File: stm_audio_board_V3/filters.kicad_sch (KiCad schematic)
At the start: 26 parts

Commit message: minor commit
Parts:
- removed C52, C53: 100n, Capacitor_SMD:C_0603_1608Metric, symbol Device:C_Small
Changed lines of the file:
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@@
   (junction (at 133.35 54.61) (diameter 0) (color 0 0 0 0)
   )
-  (junction (at 29.21 73.66) (diameter 0) (color 0 0 0 0)
-  )
   (junction (at 180.34 46.99) (diameter 0) (color 0 0 0 0)
   )
@@
   (junction (at 156.21 54.61) (diameter 0) (color 0 0 0 0)
   )
-  (junction (at 29.21 68.58) (diameter 0) (color 0 0 0 0)
-  )
-  (wire (pts (xy 29.21 68.58) (xy 38.1 68.58))
-    (stroke (width 0) (type default))
-  )
   (wire (pts (xy 109.22 48.26) (xy 109.22 46.99))
     (stroke (width 0) (type default))
@@
     (stroke (width 0) (type default))
   )
-  (wire (pts (xy 29.21 73.66) (xy 38.1 73.66))
-    (stroke (width 0) (type default))
-  )
   (wire (pts (xy 144.78 54.61) (xy 156.21 54.61))
     (stroke (width 0) (type default))
@@
     (stroke (width 0) (type default))
   )
-  (wire (pts (xy 26.67 68.58) (xy 29.21 68.58))
-    (stroke (width 0) (type default))
-  )
   (wire (pts (xy 44.45 53.34) (xy 44.45 54.61))
     (stroke (width 0) (type default))
   )
   (wire (pts (xy 133.35 54.61) (xy 144.78 54.61))
-    (stroke (width 0) (type default))
-  )
-  (wire (pts (xy 26.67 73.66) (xy 29.21 73.66))
     (stroke (width 0) (type default))
   )
@@
     )
   )
-  (symbol (lib_id "power:+9V") (at 26.67 68.58 0) (unit 1)
-    (in_bom yes) (on_board yes) (dnp no) (fields_autoplaced)
-    (property "Reference" "#PWR074" (at 26.67 72.39 0)
-      (effects (font (size 1.27 1.27)) hide)
-    )
-    (property "Value" "+9V" (at 26.67 64.77 0)
-      (effects (font (size 1.27 1.27)))
-    )
-    (property "Footprint" "" (at 26.67 68.58 0)
-      (effects (font (size 1.27 1.27)) hide)
-    )
-    (property "Datasheet" "" (at 26.67 68.58 0)
-      (effects (font (size 1.27 1.27)) hide)
-    )
-    (pin "1")
-    (instances
-      (project "stm_audio_board_V3"
-        (path "/6997cf63-2615-4e49-9471-e7da1b6bae71/2eb2ee8f-ab98-4666-97f0-bfacb073bc88"
-          (reference "#PWR074") (unit 1)
-        )
-        (path "/6997cf63-2615-4e49-9471-e7da1b6bae71/927539c8-c0d0-4950-9b67-385a1cdd80f8"
-          (reference "#PWR055") (unit 1)
-        )
-      )
-    )
-  )
   (symbol (lib_id "Device:C_Small") (at 97.79 50.8 0) (unit 1)
     (in_bom yes) (on_board yes) (dnp no) (fields_autoplaced)
@@
     )
   )
-  (symbol (lib_id "Device:C_Small") (at 38.1 71.12 0) (unit 1)
-    (in_bom yes) (on_board yes) (dnp no) (fields_autoplaced)
-    (property "Reference" "C53" (at 40.64 70.4913 0)
-      (effects (font (size 1.27 1.27)) (justify left))
-    )
-    (property "Value" "100n" (at 40.64 73.0313 0)
-      (effects (font (size 1.27 1.27)) (justify left))
-    )
-    (property "Footprint" "Capacitor_SMD:C_0603_1608Metric" (at 38.1 71.12 0)
-      (effects (font (size 1.27 1.27)) hide)
-    )
-    (property "Datasheet" "~" (at 38.1 71.12 0)
-      (effects (font (size 1.27 1.27)) hide)
-    )
-    (pin "1")
-    (pin "2")
-    (instances
-      (project "stm_audio_board_V3"
-        (path "/6997cf63-2615-4e49-9471-e7da1b6bae71"
-          (reference "C53") (unit 1)
-        )
-        (path "/6997cf63-2615-4e49-9471-e7da1b6bae71/927539c8-c0d0-4950-9b67-385a1cdd80f8"
-          (reference "C90") (unit 1)
-        )
-      )
-    )
-  )
   (symbol (lib_id "power:GND") (at 26.67 55.88 0) (unit 1)
     (in_bom yes) (on_board yes) (dnp no) (fields_autoplaced)
@@
     )
   )
-  (symbol (lib_id "Device:C_Small") (at 29.21 71.12 0) (unit 1)
-    (in_bom yes) (on_board yes) (dnp no)
-    (property "Reference" "C52" (at 31.75 70.4913 0)
-      (effects (font (size 1.27 1.27)) (justify left))
-    )
-    (property "Value" "100n" (at 31.75 73.0313 0)
-      (effects (font (size 1.27 1.27)) (justify left))
-    )
-    (property "Footprint" "Capacitor_SMD:C_0603_1608Metric" (at 29.21 71.12 0)
-      (effects (font (size 1.27 1.27)) hide)
-    )
-    (property "Datasheet" "~" (at 29.21 71.12 0)
-      (effects (font (size 1.27 1.27)) hide)
-    )
-    (pin "1")
-    (pin "2")
-    (instances
-      (project "stm_audio_board_V3"
-        (path "/6997cf63-2615-4e49-9471-e7da1b6bae71"
-          (reference "C52") (unit 1)
-        )
-        (path "/6997cf63-2615-4e49-9471-e7da1b6bae71/927539c8-c0d0-4950-9b67-385a1cdd80f8"
-          (reference "C89") (unit 1)
-        )
-      )
-    )
-  )
   (symbol (lib_id "Device:C_Small") (at 167.64 50.8 0) (unit 1)
     (in_bom yes) (on_board yes) (dnp no)
@@
         )
       )
-    )
-  )
-  (symbol (lib_id "power:GND") (at 26.67 73.66 0) (unit 1)
-    (in_bom yes) (on_board yes) (dnp no) (fields_autoplaced)
-    (property "Reference" "#PWR05" (at 26.67 80.01 0)
-      (effects (font (size 1.27 1.27)) hide)
-    )
-    (property "Value" "GND" (at 26.67 78.74 0)
-      (effects (font (size 1.27 1.27)))
-    )
-    (property "Footprint" "" (at 26.67 73.66 0)
-      (effects (font (size 1.27 1.27)) hide)
-    )
-    (property "Datasheet" "" (at 26.67 73.66 0)
-      (effects (font (size 1.27 1.27)) hide)
-    )
-    (pin "1")
-    (instances
-      (project "stm_audio_board_V3"
-        (path "/6997cf63-2615-4e49-9471-e7da1b6bae71"
-          (reference "#PWR05") (unit 1)
-        )
-        (path "/6997cf63-2615-4e49-9471-e7da1b6bae71/927539c8-c0d0-4950-9b67-385a1cdd80f8"
-          (reference "#PWR059") (unit 1)
-        )
-      )

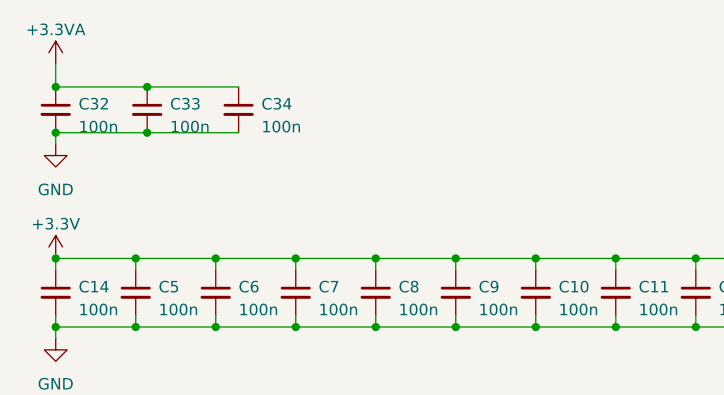
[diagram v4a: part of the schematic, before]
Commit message: gnd vias added, footswitch mux connected
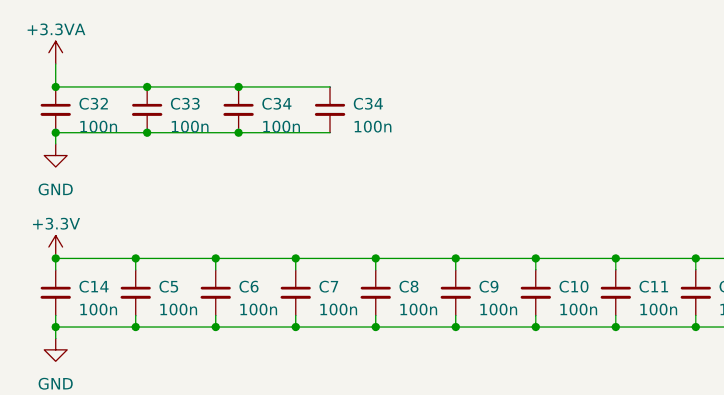
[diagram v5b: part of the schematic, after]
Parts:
- added C34: 100n, Capacitor_SMD:C_0603_1608Metric, symbol Device:C_Small
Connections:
- net +3.3VA: now also C34.1
- net GND: now also C34.2
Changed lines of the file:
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@@
   (junction (at 144.78 54.61) (diameter 0) (color 0 0 0 0)
   )
+  (junction (at 46.99 33.02) (diameter 0) (color 0 0 0 0)
+  )
   (junction (at 156.21 46.99) (diameter 0) (color 0 0 0 0)
   )
@@
   (junction (at 35.56 46.99) (diameter 0) (color 0 0 0 0)
   )
+  (junction (at 46.99 27.94) (diameter 0) (color 0 0 0 0)
+  )
   (junction (at 44.45 46.99) (diameter 0) (color 0 0 0 0)
   )
@@
     (stroke (width 0) (type default))
   )
+  (wire (pts (xy 46.99 33.02) (xy 57.15 33.02))
+    (stroke (width 0) (type default))
+  )
   (wire (pts (xy 53.34 48.26) (xy 53.34 46.99))
     (stroke (width 0) (type default))
@@
   )
   (wire (pts (xy 35.56 53.34) (xy 35.56 54.61))
+    (stroke (width 0) (type default))
+  )
+  (wire (pts (xy 46.99 27.94) (xy 57.15 27.94))
     (stroke (width 0) (type default))
   )
@@
         )
       )
+    )
+  )
+  (symbol (lib_id "Device:C_Small") (at 57.15 30.48 0) (unit 1)
+    (in_bom yes) (on_board yes) (dnp no) (fields_autoplaced)
+    (property "Reference" "C34" (at 59.69 29.8513 0)
+      (effects (font (size 1.27 1.27)) (justify left))
+    )
+    (property "Value" "100n" (at 59.69 32.3913 0)
+      (effects (font (size 1.27 1.27)) (justify left))
+    )
+    (property "Footprint" "Capacitor_SMD:C_0603_1608Metric" (at 57.15 30.48 0)
+      (effects (font (size 1.27 1.27)) hide)
+    )
+    (property "Datasheet" "~" (at 57.15 30.48 0)
+      (effects (font (size 1.27 1.27)) hide)
+    )
+    (pin "1")
+    (pin "2")
+    (instances
+      (project "stm_audio_board_V3"
+        (path "/6997cf63-2615-4e49-9471-e7da1b6bae71"
+          (reference "C34") (unit 1)
+        )
+        (path "/6997cf63-2615-4e49-9471-e7da1b6bae71/927539c8-c0d0-4950-9b67-385a1cdd80f8"
+          (reference "C217") (unit 1)
+        )
+      )
